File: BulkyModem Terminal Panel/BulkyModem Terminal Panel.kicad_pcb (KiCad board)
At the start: 2 copper layers, 100 x 23.2 mm, 16 parts, among them J1 Front Panel, M1 Mounting_Pin, M2 Mounting_Pin, M3 Mounting_Pin, M4 Mounting_Pin, SW1 MODE, SW2 POW, SW3 DEFAULT, SW4 RESET

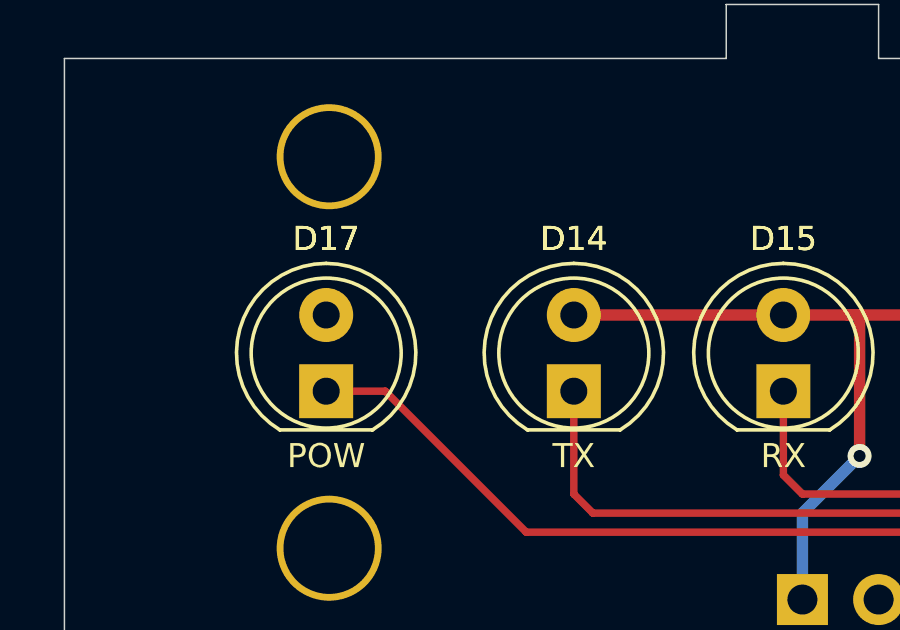
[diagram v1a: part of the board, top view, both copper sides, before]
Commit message: Missing a trace
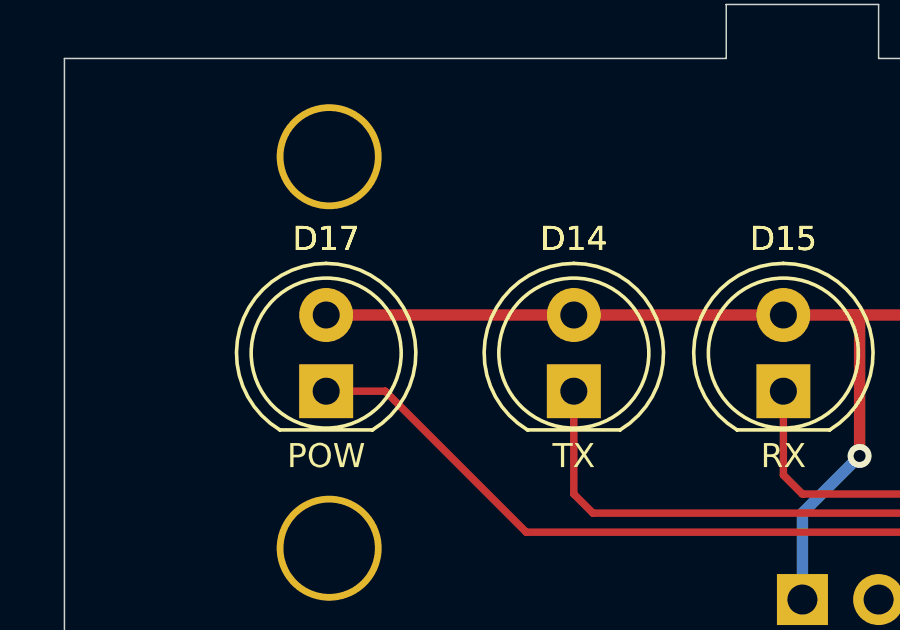
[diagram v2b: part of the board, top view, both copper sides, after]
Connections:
- J1 pad 3: /LED.POW -> /LED.5V
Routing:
- net VCC: track 120.2 -> 128.5 mm
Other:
- board text added: "BulkyModem Terminal Panel (rev. B) github.com/tebl"
- board text removed: "BulkyModem Terminal Panel (rev. A) github.com/tebl"
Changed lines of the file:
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@@
 	(net 24 "unconnected-(J1-N.C.-Pad14)")
 	(net 25 "unconnected-(J1-N.C.-Pad11)")
-	(net 26 "/LED.POW")
 	(footprint "mounting:M3_pin"
 		(layer "F.Cu")
@@
 			(layers "*.Cu" "*.Mask")
 			(remove_unused_layers no)
-			(net 26 "/LED.POW")
+			(net 9 "/LED.5V")
 			(pinfunction "LED_POW")
 			(pintype "passive")
@@
 		(layer "Edge.Cuts")
 	)
-	(gr_text "BulkyModem\nTerminal Panel (rev. A)\ngithub.com/tebl"
+	(gr_text "BulkyModem\nTerminal Panel (rev. B)\ngithub.com/tebl"
 		(at 94.1 122.849 270)
 		(layer "B.SilkS")
@@
 		(width 0.381)
 		(layer "F.Cu")
+		(net 2)
+	)
+	(segment
+		(start 108.07 121.325)
+		(end 99.815 121.325)
+		(width 0.381)
+		(layer "F.Cu")

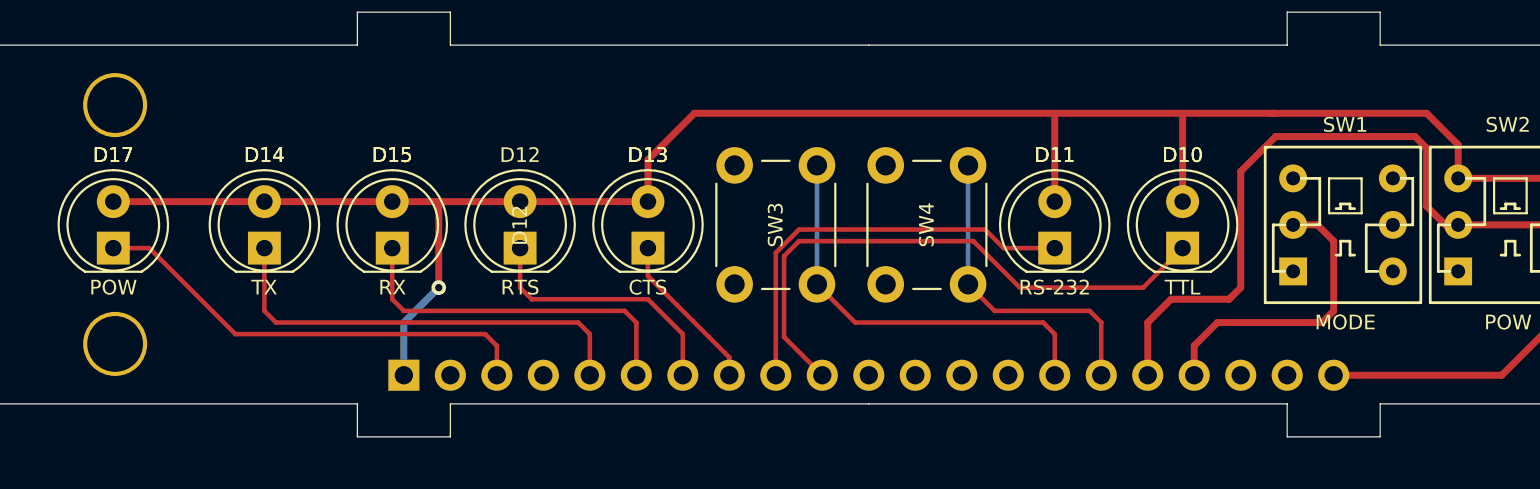
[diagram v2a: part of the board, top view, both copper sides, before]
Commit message: Flipped serial LEDs
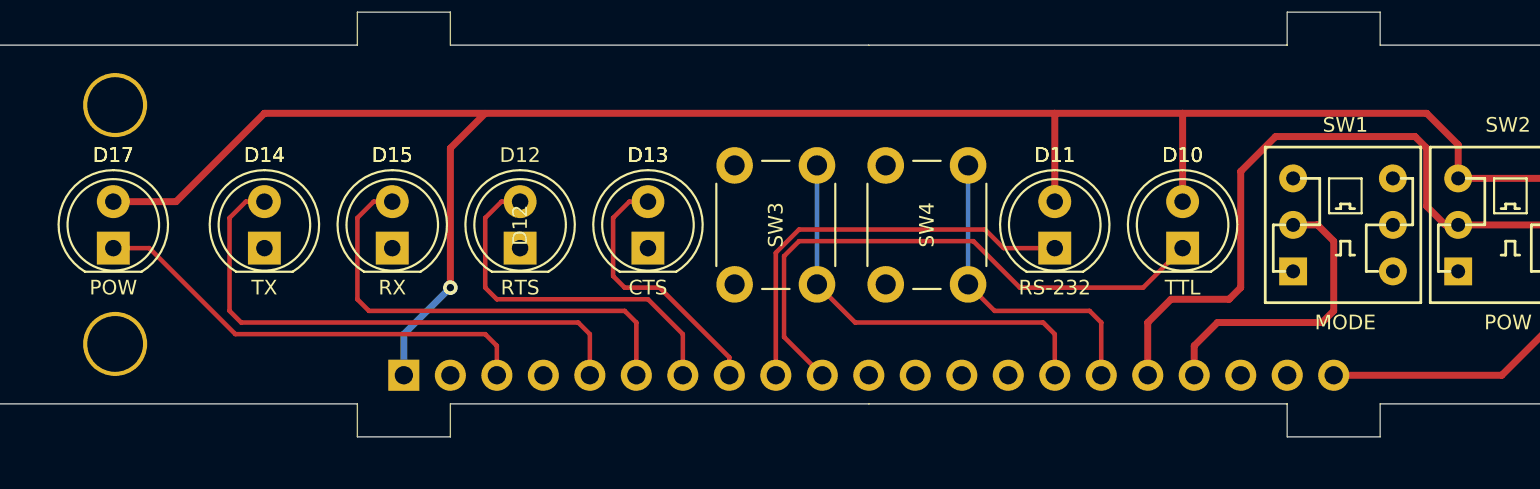
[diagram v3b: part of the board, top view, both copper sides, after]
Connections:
- D12 pad 1: /LED.RTS -> GND
- D12 pad 2: VCC -> /LED.RTS
- D13 pad 1: /LED.CTS -> GND
- D13 pad 2: VCC -> /LED.CTS
- D14 pad 1: /LED.TX -> GND
- D14 pad 2: VCC -> /LED.TX
- D15 pad 1: /LED.RX -> GND
- D15 pad 2: VCC -> /LED.RX
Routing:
- net /LED.CTS: track 8.79 -> 14.6 mm
- net /LED.RTS: track 14.3 -> 20.2 mm
- net /LED.RX: track 19.5 -> 25.4 mm
- net /LED.TX: track 24.0 -> 29.8 mm
- net VCC: track 128.5 -> 132.4 mm
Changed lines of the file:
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@@
 			(layers "*.Cu" "*.Mask")
 			(remove_unused_layers no)
-			(net 5 "/LED.RTS")
+			(net 1 "GND")
 			(pinfunction "K")
 			(pintype "passive")
@@
 			(layers "*.Cu" "*.Mask")
 			(remove_unused_layers no)
-			(net 2 "VCC")
+			(net 5 "/LED.RTS")
 			(pinfunction "A")
 			(pintype "passive")
@@
 			(layers "*.Cu" "*.Mask")
 			(remove_unused_layers no)
-			(net 6 "/LED.CTS")
+			(net 1 "GND")
 			(pinfunction "K")
 			(pintype "passive")
@@
 			(layers "*.Cu" "*.Mask")
 			(remove_unused_layers no)
-			(net 2 "VCC")
+			(net 6 "/LED.CTS")
 			(pinfunction "A")
 			(pintype "passive")
@@
 			(layers "*.Cu" "*.Mask")
 			(remove_unused_layers no)
-			(net 8 "/LED.RX")
+			(net 1 "GND")
 			(pinfunction "K")
 			(pintype "passive")
@@
 			(layers "*.Cu" "*.Mask")
 			(remove_unused_layers no)
-			(net 2 "VCC")
+			(net 8 "/LED.RX")
 			(pinfunction "A")
 			(pintype "passive")
@@
 			(layers "*.Cu" "*.Mask")
 			(remove_unused_layers no)
-			(net 7 "/LED.TX")
+			(net 1 "GND")
 			(pinfunction "K")
 			(pintype "passive")
@@
 			(layers "*.Cu" "*.Mask")
 			(remove_unused_layers no)
-			(net 2 "VCC")
+			(net 7 "/LED.TX")
 			(pinfunction "A")
 			(pintype "passive")
@@
 	)
 	(segment
-		(start 163.315 116.499)
+		(start 158.235 116.499)
 		(end 171.57 116.499)
 		(width 0.381)
@@
 	)
 	(segment
-		(start 163.315 116.499)
-		(end 158.235 116.499)
-		(width 0.381)
-		(layer "F.Cu")
-		(net 2)
-	)
-	(segment
-		(start 115.69 121.325)
-		(end 108.07 121.325)
-		(width 0.381)
-		(layer "F.Cu")
-		(net 2)
-	)
-	(segment
 		(start 158.235 116.499)
 		(end 151.25 116.499)
@@
 	)
 	(segment
-		(start 117.595 126.024)
-		(end 117.595 121.325)
+		(start 118.23 118.404)
+		(end 120.135 116.499)
 		(width 0.381)
 		(layer "F.Cu")
@@
 	)
 	(segment
-		(start 108.07 121.325)
-		(end 99.815 121.325)
-		(width 0.381)
-		(layer "F.Cu")
-		(net 2)
-	)
-	(segment
-		(start 117.595 121.325)
-		(end 117.214 121.325)
+		(start 108.07 116.499)
+		(end 103.244 121.325)
 		(width 0.381)
 		(layer "F.Cu")
@@
 	)
 	(segment
-		(start 131.565 116.499)
-		(end 129.025 119.039)
-		(width 0.381)
-		(layer "F.Cu")
-		(net 2)
-	)
-	(segment
-		(start 163.061 116.499)
-		(end 163.315 116.499)
-		(width 0.381)
-		(layer "F.Cu")
-		(net 2)
-	)
-	(segment
 		(start 151.25 121.325)
 		(end 151.25 116.499)
@@
 	)
 	(segment
-		(start 129.025 121.325)
-		(end 117.214 121.325)
+		(start 108.07 116.499)
+		(end 151.25 116.499)
 		(width 0.381)
 		(layer "F.Cu")
@@
 	)
 	(segment
-		(start 117.214 121.325)
-		(end 115.69 121.325)
+		(start 103.244 121.325)
+		(end 99.815 121.325)
 		(width 0.381)
 		(layer "F.Cu")
@@
 	)
 	(segment
-		(start 151.25 116.499)
-		(end 131.565 116.499)
-		(width 0.381)
-		(layer "F.Cu")
-		(net 2)
-	)
-	(segment
-		(start 129.025 119.039)
-		(end 129.025 121.325)
+		(start 118.23 126.024)
+		(end 118.23 118.404)
 		(width 0.381)
 		(layer "F.Cu")
@@
 	)
 	(via
-		(at 117.595 126.024)
+		(at 118.23 126.024)
 		(size 0.8)
 		(drill 0.4)
@@
 	)
 	(segment
-		(start 115.69 130.81)
-		(end 115.69 127.929)
+		(start 118.23 126.024)
+		(end 115.69 128.564)
 		(width 0.381)
 		(layer "B.Cu")
@@
 	)
 	(segment
-		(start 115.69 127.929)
-		(end 117.595 126.024)
+		(start 115.69 128.564)
+		(end 115.69 130.81)
 		(width 0.381)
 		(layer "B.Cu")
@@
 	)
 	(segment
-		(start 122.04 123.865)
-		(end 122.04 126.024)
+		(start 122.04 121.325)
+		(end 121.024 121.325)
 		(width 0.25)
 		(layer "F.Cu")
@@
 	)
 	(segment
-		(start 122.04 126.024)
-		(end 122.675 126.659)
+		(start 120.77 126.659)
+		(end 129.025 126.659)
 		(width 0.25)
 		(layer "F.Cu")
@@
 	)
 	(segment
-		(start 122.675 126.659)
-		(end 129.025 126.659)
+		(start 120.135 122.214)
+		(end 120.135 126.024)
+		(width 0.25)
+		(layer "F.Cu")
+		(net 5)
+	)
+	(segment
+		(start 121.024 121.325)
+		(end 120.135 122.214)
 		(width 0.25)
 		(layer "F.Cu")
@@
 	)
 	(segment
-		(start 129.025 123.865)
-		(end 129.025 125.389)
+		(start 120.135 126.024)
+		(end 120.77 126.659)
+		(width 0.25)
+		(layer "F.Cu")
+		(net 5)
+	)
+	(segment
+		(start 129.025 121.325)
+		(end 128.009 121.325)
+		(width 0.25)
+		(layer "F.Cu")
+		(net 6)
+	)
+	(segment
+		(start 127.12 122.214)
+		(end 127.12 125.389)
+		(width 0.25)
+		(layer "F.Cu")
+		(net 6)
+	)
+	(segment
+		(start 128.009 121.325)
+		(end 127.12 122.214)
+		(width 0.25)
+		(layer "F.Cu")
+		(net 6)
+	)
+	(segment
+		(start 129.66 126.024)
+		(end 133.47 129.834)
 		(width 0.25)
 		(layer "F.Cu")
@@
 	)
 	(segment
-		(start 129.025 125.389)
-		(end 133.47 129.834)
+		(start 127.12 125.389)
+		(end 127.755 126.024)
 		(width 0.25)
 		(layer "F.Cu")
@@
 	)
 	(segment
-		(start 108.705 127.929)
-		(end 125.215 127.929)
+		(start 127.755 126.024)
+		(end 129.66 126.024)
+		(width 0.25)
+		(layer "F.Cu")
+		(net 6)
+	)
+	(segment
+		(start 107.054 121.325)
+		(end 106.165 122.214)
 		(width 0.25)
 		(layer "F.Cu")
@@
 	)
 	(segment
-		(start 108.07 127.294)
-		(end 108.705 127.929)
+		(start 106.165 122.214)
+		(end 106.165 127.294)
 		(width 0.25)
 		(layer "F.Cu")
@@
 	)
 	(segment
+		(start 106.165 127.294)
+		(end 106.8 127.929)
+		(width 0.25)
+		(layer "F.Cu")
+		(net 7)
+	)
+	(segment
+		(start 106.8 127.929)
+		(end 125.215 127.929)
+		(width 0.25)
+		(layer "F.Cu")
+		(net 7)
+	)
+	(segment
 		(start 125.215 127.929)
 		(end 125.85 128.564)
@@
 	)
 	(segment
-		(start 108.07 123.865)
-		(end 108.07 127.294)
+		(start 108.07 121.325)
+		(end 107.054 121.325)
 		(width 0.25)
 		(layer "F.Cu")
@@
 	)
 	(segment
-		(start 115.69 127.294)
+		(start 113.785 127.294)
 		(end 127.755 127.294)
 		(width 0.25)
@@
 	)
 	(segment
-		(start 115.055 126.659)
-		(end 115.69 127.294)
+		(start 113.15 126.659)
+		(end 113.785 127.294)
 		(width 0.25)
 		(layer "F.Cu")
@@
 	)
 	(segment
-		(start 115.055 123.865)
-		(end 115.055 126.659)
+		(start 113.15 122.214)
+		(end 113.15 126.659)
+		(width 0.25)
+		(layer "F.Cu")
+		(net 8)
+	)
+	(segment
+		(start 114.039 121.325)
+		(end 113.15 122.214)
 		(width 0.25)
 		(layer "F.Cu")
@@
 		(width 0.25)
 		(layer "F.Cu")
+		(net 8)
+	)
+	(segment
+		(start 115.055 121.325)
+		(end 114.039 121.325)
+		(width 0.25)
+		(layer "F.Cu")
